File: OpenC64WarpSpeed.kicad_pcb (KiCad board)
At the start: 2 copper layers, 58.4 x 61.7 mm, 17 parts, among them P1 C64-Exp-Port, SW1 SW_C64_C128, SW2 SW_Push, U1 74LS109, U2 27128

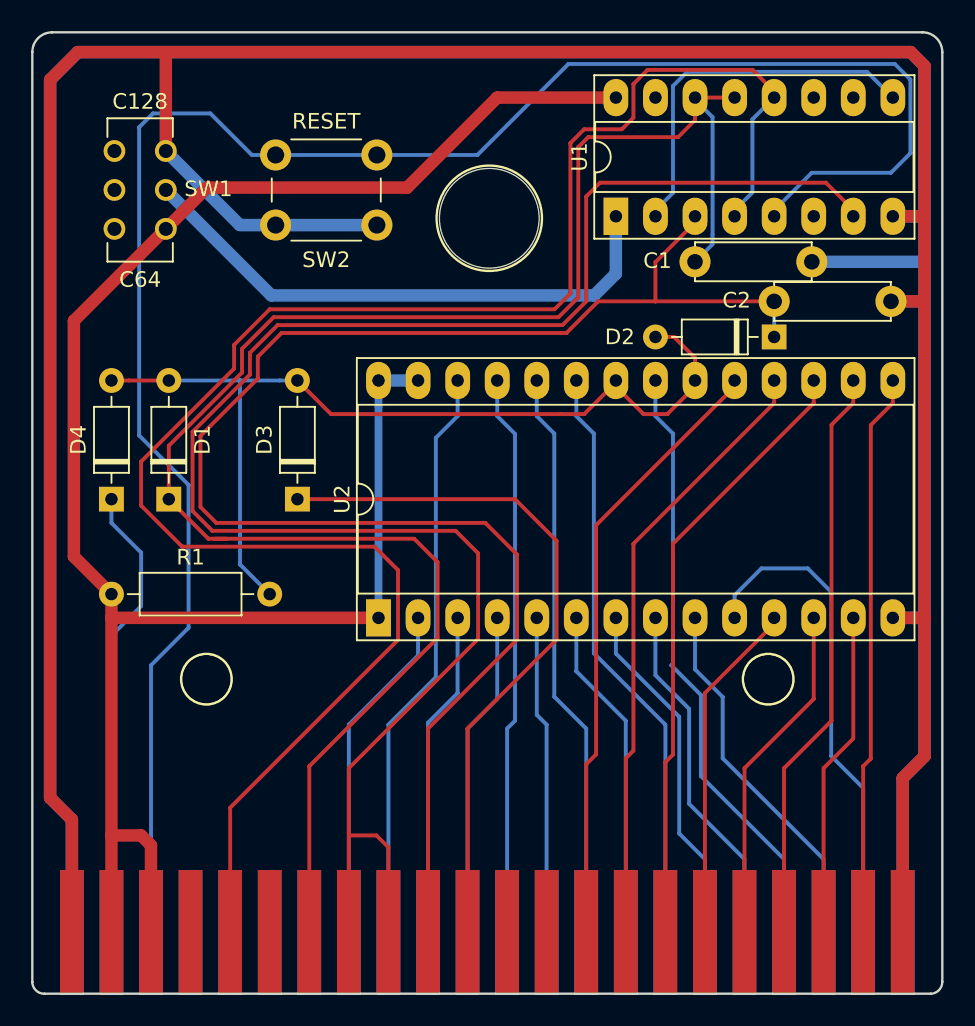
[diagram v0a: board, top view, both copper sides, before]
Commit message: Minor fixes and add license claim
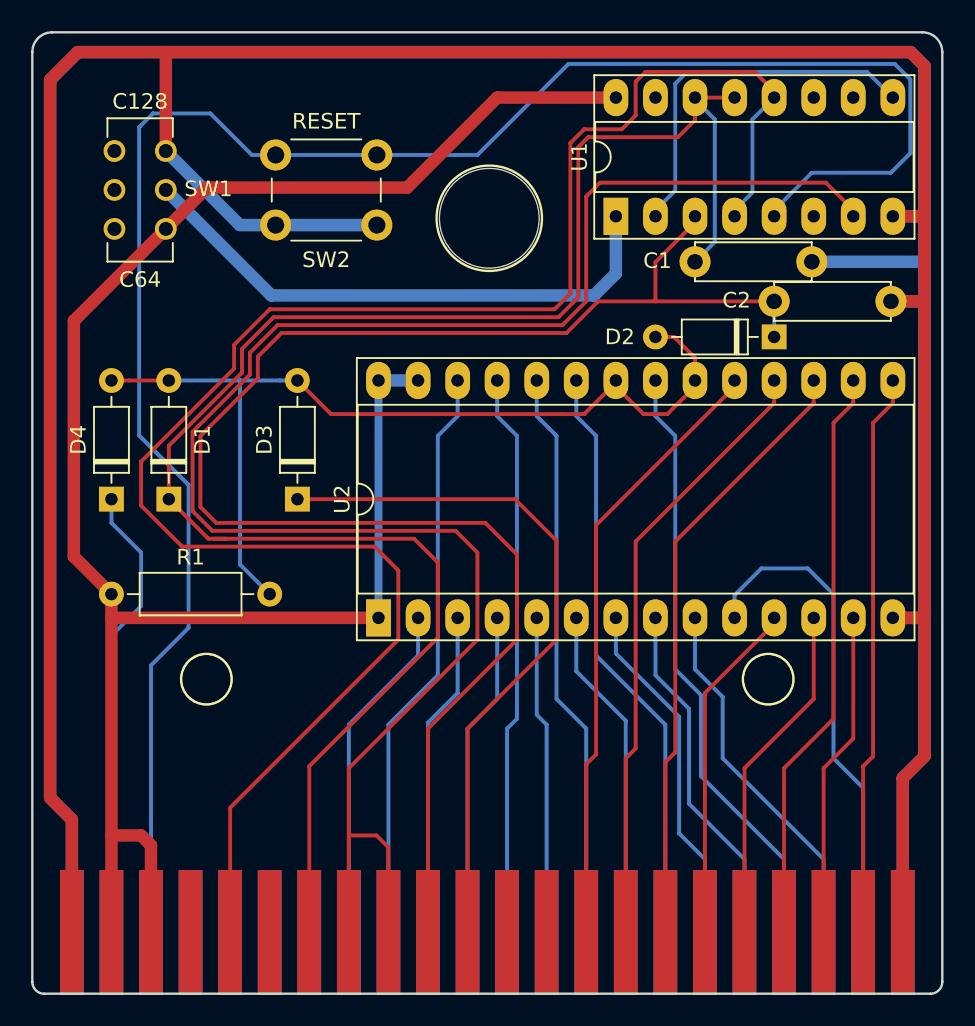
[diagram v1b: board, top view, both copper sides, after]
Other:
- board text added: "Licensed under CERN OHL v.1.2"

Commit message: Change version number
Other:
- board text added: "V1ORIG"
- board text removed: "V1"
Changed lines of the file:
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@@
       (padsonsilk false)
       (subtractmaskfromsilk false)
-      (outputformat 3)
+      (outputformat 1)
       (mirror false)
-      (drillshape 2)
+      (drillshape 0)
       (scaleselection 1)
-      (outputdirectory "dxf"))
+      (outputdirectory "gerbers"))
   )
   (net 0 "")
@@
     (arrow2b (pts (xy 115.57 144.78) (xy 116.696504 144.193579)))
   )
-  (gr_text V1 (at 62.23 120.396) (layer B.SilkS)
+  (gr_text V1ORIG (at 63.627 120.396) (layer B.SilkS)
     (effects (font (size 1 1) (thickness 0.15)) (justify mirror))
   )

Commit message: Fix capacitor value: 470nF -> 47pF - Thanks @svenpetersen1965
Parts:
- removed G***: LOGO, OpenC64WarpSpeed:Bottom
- removed G***: LOGO, OpenC64WarpSpeed:Top
- C1, C2: value 470n -> 47p
